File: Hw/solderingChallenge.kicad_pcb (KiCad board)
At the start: 2 copper layers, 13 parts, among them U1 ATtiny85-20SU

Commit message: Update connections
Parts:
- added J1: ISP, Connector_PinHeader_2.54mm:PinHeader_2x03_P2.54mm_Vertical, F.Cu at (139.9, 92.3)
- added TP1: PB0, TestPoint:TestPoint_Pad_1.0x1.0mm, F.Cu at (142.1, 81.2)
- added TP10: GND, Connectors_EC:TestPoint_Pad_1.0x1.0mm, F.Cu at (155.5, 73.5)
- added TP2: PB1, Connectors_EC:TestPoint_Pad_1.0x1.0mm, F.Cu at (142.1, 78.8)
- added TP3: PB2, Connectors_EC:TestPoint_Pad_1.0x1.0mm, F.Cu at (142.1, 75.7)
- added TP4: PB3, Connectors_EC:TestPoint_Pad_1.0x1.0mm, F.Cu at (142.1, 83.6)
- added TP5: PB4, Connectors_EC:TestPoint_Pad_1.0x1.0mm, F.Cu at (142.1, 86.2)
- added TP6: GND, Connectors_EC:TestPoint_Pad_1.0x1.0mm, F.Cu at (153.5, 83.5)
- added TP7: GND, Connectors_EC:TestPoint_Pad_1.0x1.0mm, F.Cu at (153.5, 77.1)
- added TP8: GND, Connectors_EC:TestPoint_Pad_1.0x1.0mm, F.Cu at (153.5, 80.6)
- added TP9: GND, Connectors_EC:TestPoint_Pad_1.0x1.0mm, F.Cu at (153.5, 86.1)
- moved D1 6.29 mm to (144.5, 73.6), turned to 180 degrees
- moved D2 6.29 mm to (144.5, 77.1), turned to 180 degrees
- moved D3 6.29 mm to (144.5, 80.6), turned to 180 degrees
- moved D4 6.29 mm to (144.5, 83.6), turned to 180 degrees
- moved D5 6.29 mm to (144.5, 86.1), turned to 180 degrees
- moved R1 6.29 mm to (150.5, 73.6), turned to 180 degrees
- moved R2 6.29 mm to (150.5, 77.1), turned to 180 degrees
- moved R3 6.29 mm to (150.5, 80.6), turned to 180 degrees
- moved R4 6.29 mm to (150.5, 83.6), turned to 180 degrees
- moved R5 6.29 mm to (150.5, 86.1), turned to 180 degrees
- moved C1 1.81 mm to (138.2, 73.7)
- moved BT1 1.41 mm to (142.4, 79.2)
- moved U1 1.27 mm to (135.9, 78.8)
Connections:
- net /PB1 renamed /MISO
- D1 pad 2: /PB0 -> /PB2
- D3 pad 2: /PB2 -> /MOSI
- U1 pad 5: /PB0 -> /MOSI
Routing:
- net VCC: track 0.00 -> 75.1 mm, vias 0 -> 2
- net /PB2: track 0.00 -> 34.5 mm, vias 0 -> 2
- net /RST: track 0.00 -> 32.3 mm, vias 0 -> 2
- net /MISO: track 0.00 -> 31.0 mm, vias 0 -> 2
- net GND: track 0.00 -> 20.7 mm, vias 0 -> 5
- net /PB3: track 0.00 -> 18.5 mm
- net /MOSI: track 0.00 -> 16.8 mm, vias 0 -> 2
- net /PB4: track 0.00 -> 16.2 mm
- net Net-(D5-Pad1): track 0.00 -> 5.36 mm
- net Net-(D4-Pad1): track 0.00 -> 5.03 mm
- net Net-(D3-Pad1): track 0.00 -> 4.25 mm
- net Net-(D2-Pad1): track 0.00 -> 3.97 mm
- net Net-(D1-Pad1): track 0.00 -> 3.05 mm
- added copper zone on B.Cu, net GND
- added copper zone on F.Cu, net GND
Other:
- board outline added: 33.5 x 33.5 mm
- net class Default: trace_width 0.25 -> 0.35; via_dia 0.8 -> 1; via_drill 0.4 -> 0.6
- net class vcc added: clearance 0.3, trace_width 0.5, via_dia 1, via_drill 0.6
- rule trace_min: 0.2 -> 0.3
- board text added: "0201"
- board text added: "0402"
- board text added: "0603"
- board text added: "0805"
- board text added: "1206"

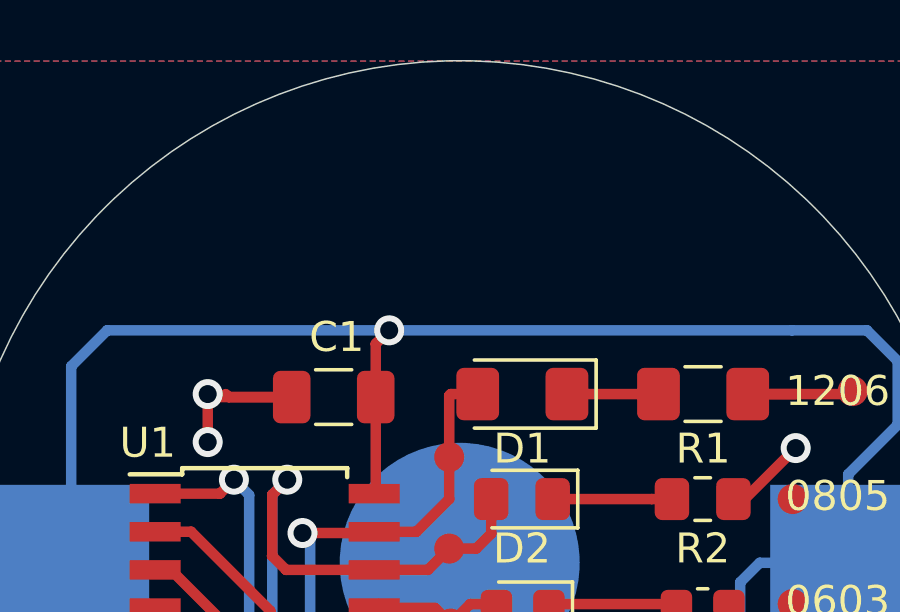
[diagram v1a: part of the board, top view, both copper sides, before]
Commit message: add logo wurth
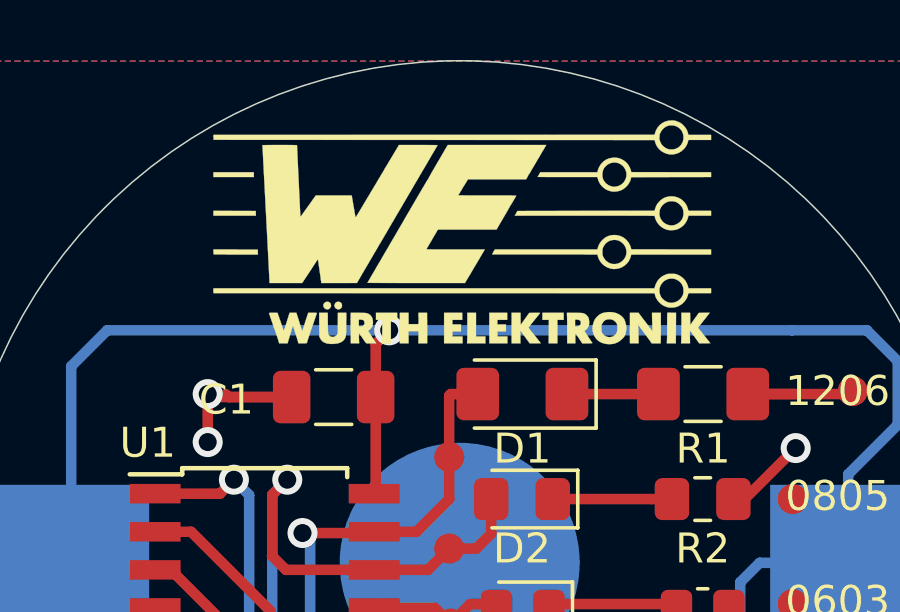
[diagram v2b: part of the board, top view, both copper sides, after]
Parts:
- added G***: LOGO, Aesthetics:wurth, F.Cu at (142.5, 68.2)

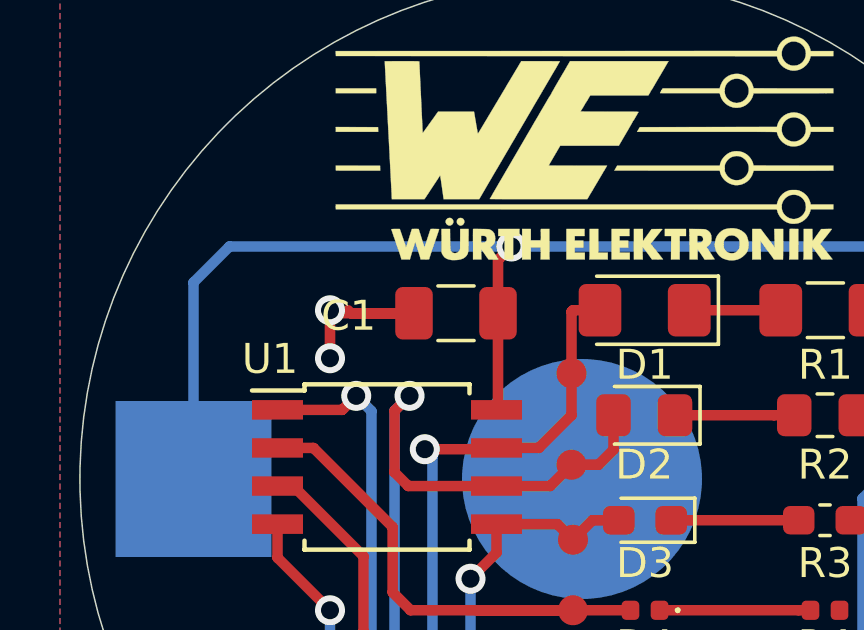
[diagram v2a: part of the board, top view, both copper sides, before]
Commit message: Change capacitor size
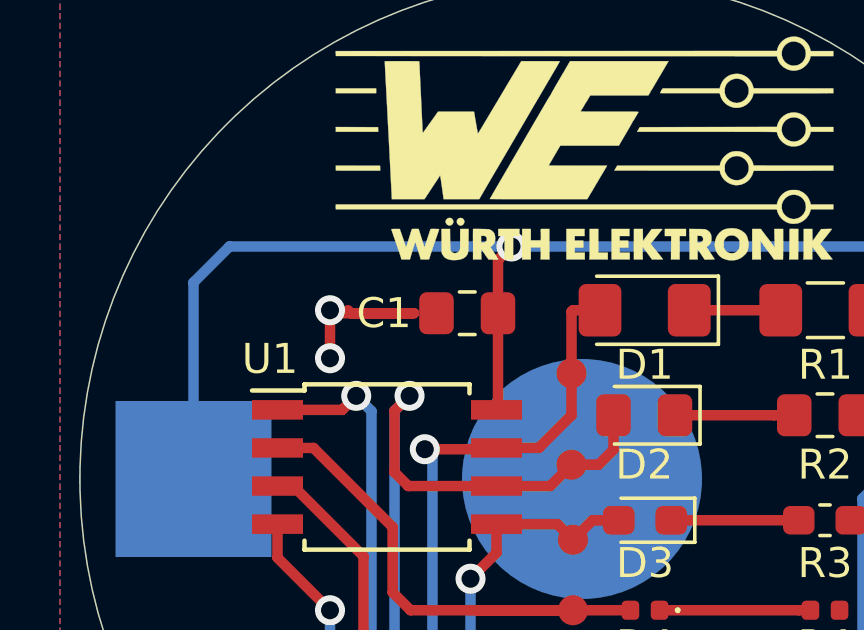
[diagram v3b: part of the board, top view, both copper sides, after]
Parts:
- C1: footprint Capacitor_SMD:C_1206_3216Metric -> Capacitor_SMD:C_0805_2012Metric_Pad1.15x1.40mm_HandSolder
- moved C1 0.38 mm to (138.6, 73.7)
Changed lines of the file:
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@@
-(kicad_pcb (version 20171130) (host pcbnew "(5.0.1-3-g963ef8bb5)")
+(kicad_pcb (version 20171130) (host pcbnew "(5.1.0-0)")
   (general
     (thickness 1.6)
@@
     (zone_45_only no)
     (trace_min 0.3)
-    (segment_width 0.2)
-    (edge_width 0.05)
     (via_size 1)
     (via_drill 0.6)
@@
     (uvia_min_size 0.2)
     (uvia_min_drill 0.1)
+    (edge_width 0.05)
+    (segment_width 0.2)
     (pcb_text_width 0.3)
     (pcb_text_size 1.5 1.5)
@@
     (uvia_dia 0.3)
     (uvia_drill 0.1)
+    (diff_pair_width 0.3)
     (diff_pair_gap 0.3)
-    (diff_pair_width 0.3)
     (add_net /MISO)
     (add_net /MOSI)
@@
     (uvia_dia 0.3)
     (uvia_drill 0.1)
+    (diff_pair_width 0.3)
     (diff_pair_gap 0.3)
-    (diff_pair_width 0.3)
+  )
+  (module Capacitor_SMD:C_0805_2012Metric_Pad1.15x1.40mm_HandSolder (layer F.Cu)
+    (at 138.575 73.7 180)
+    (descr "Capacitor SMD 0805 (2012 Metric), square (rectangular) end terminal, IPC_7351 nominal with elongated pad for handsoldering. (Body size source: https://docs.google.com/spreadsheets/d/1BsfQQcO9C6DZCsRaXUlFlo91Tg2WpOkGARC1WS5S8t0/edit?usp=sharing), generated with kicad-footprint-generator")
+    (tags "capacitor handsolder")
+    (attr smd)
+    (fp_text reference C1 (at 2.775 0 180) (layer F.SilkS)
+      (effects (font (size 1 1) (thickness 0.15)))
+    )
+    (fp_text value 0.1uF (at 0 1.65 180) (layer F.Fab)
+      (effects (font (size 1 1) (thickness 0.15)))
+    )
+    (fp_text user %R (at 0 0 180) (layer F.Fab)
+      (effects (font (size 0.5 0.5) (thickness 0.08)))
+    )
+    (fp_line (start 1.85 0.95) (end -1.85 0.95) (layer F.CrtYd) (width 0.05))
+    (fp_line (start 1.85 -0.95) (end 1.85 0.95) (layer F.CrtYd) (width 0.05))
+    (fp_line (start -1.85 -0.95) (end 1.85 -0.95) (layer F.CrtYd) (width 0.05))
+    (fp_line (start -1.85 0.95) (end -1.85 -0.95) (layer F.CrtYd) (width 0.05))
+    (fp_line (start -0.261252 0.71) (end 0.261252 0.71) (layer F.SilkS) (width 0.12))
+    (fp_line (start -0.261252 -0.71) (end 0.261252 -0.71) (layer F.SilkS) (width 0.12))
+    (fp_line (start 1 0.6) (end -1 0.6) (layer F.Fab) (width 0.1))
+    (fp_line (start 1 -0.6) (end 1 0.6) (layer F.Fab) (width 0.1))
+    (fp_line (start -1 -0.6) (end 1 -0.6) (layer F.Fab) (width 0.1))
+    (fp_line (start -1 0.6) (end -1 -0.6) (layer F.Fab) (width 0.1))
+    (pad 2 smd roundrect (at 1.025 0 180) (size 1.15 1.4) (layers F.Cu F.Paste F.Mask) (roundrect_rratio 0.217391)
+      (net 9 GND))
+    (pad 1 smd roundrect (at -1.025 0 180) (size 1.15 1.4) (layers F.Cu F.Paste F.Mask) (roundrect_rratio 0.217391)
+      (net 11 VCC))
+    (model ${KISYS3DMOD}/Capacitor_SMD.3dshapes/C_0805_2012Metric.wrl
+      (at (xyz 0 0 0))
+      (scale (xyz 1 1 1))
+      (rotate (xyz 0 0 0))
+    )
   )
   (module Connectors_EC:TestPoint_Pad_1.0x1.0mm (layer F.Cu)
@@
     )
   )
-  (module Capacitor_SMD:C_1206_3216Metric (layer F.Cu)
-    (at 138.2 73.7 180)
-    (descr "Capacitor SMD 1206 (3216 Metric), square (rectangular) end terminal, IPC_7351 nominal, (Body size source: http://www.tortai-tech.com/upload/download/2011102023233369053.pdf), generated with kicad-footprint-generator")
-    (tags capacitor)
-    (attr smd)
-    (fp_text reference C1 (at 3.58 -0.087 180) (layer F.SilkS)
-      (effects (font (size 1 1) (thickness 0.15)))
-    )
-    (fp_text value 0.1uF (at 0 1.82 180) (layer F.Fab)
-      (effects (font (size 1 1) (thickness 0.15)))
-    )
-    (fp_line (start -1.6 0.8) (end -1.6 -0.8) (layer F.Fab) (width 0.1))
-    (fp_line (start -1.6 -0.8) (end 1.6 -0.8) (layer F.Fab) (width 0.1))
-    (fp_line (start 1.6 -0.8) (end 1.6 0.8) (layer F.Fab) (width 0.1))
-    (fp_line (start 1.6 0.8) (end -1.6 0.8) (layer F.Fab) (width 0.1))
-    (fp_line (start -0.602064 -0.91) (end 0.602064 -0.91) (layer F.SilkS) (width 0.12))
-    (fp_line (start -0.602064 0.91) (end 0.602064 0.91) (layer F.SilkS) (width 0.12))
-    (fp_line (start -2.28 1.12) (end -2.28 -1.12) (layer F.CrtYd) (width 0.05))
-    (fp_line (start -2.28 -1.12) (end 2.28 -1.12) (layer F.CrtYd) (width 0.05))
-    (fp_line (start 2.28 -1.12) (end 2.28 1.12) (layer F.CrtYd) (width 0.05))
-    (fp_line (start 2.28 1.12) (end -2.28 1.12) (layer F.CrtYd) (width 0.05))
-    (fp_text user %R (at 0 0 180) (layer F.Fab)
-      (effects (font (size 0.8 0.8) (thickness 0.12)))
-    )
-    (pad 1 smd roundrect (at -1.4 0 180) (size 1.25 1.75) (layers F.Cu F.Paste F.Mask) (roundrect_rratio 0.2)
-      (net 11 VCC))
-    (pad 2 smd roundrect (at 1.4 0 180) (size 1.25 1.75) (layers F.Cu F.Paste F.Mask) (roundrect_rratio 0.2)
-      (net 9 GND))
-    (model ${KISYS3DMOD}/Capacitor_SMD.3dshapes/C_1206_3216Metric.wrl
-      (at (xyz 0 0 0))
-      (scale (xyz 1 1 1))
-      (rotate (xyz 0 0 0))
-    )
-  )

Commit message: Update version
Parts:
- removed D5: 0201, LED_SMD:LED_0201_0603Metric
- removed the G*** at (142.5, 68.2)
- removed R5: 0201, Resistor_SMD:R_0201_0603Metric
- removed TP5: PB4, Connectors_EC:TestPoint_Pad_1.0x1.0mm
- removed TP9: GND, Connectors_EC:TestPoint_Pad_1.0x1.0mm
- added G***: LOGO, Aesthetics:wurth, B.Cu at (133.6, 88.9)
- added G***: LOGO, Aesthetics:wurth, F.Cu at (133.3, 85.2)
- added G***: LOGO, Aesthetics:electronic_cats_logo_4x3, F.Cu at (150.4, 88.2)
- added G***: LOGO, Aesthetics:makersGDL, B.Cu at (142.0, 65.1)
- added G***: LOGO, Aesthetics:mouser, B.Cu at (151.4, 89.1)
- added G***: LOGO, Aesthetics:mouser, F.Cu at (137.8, 69.1)
- added G***: LOGO, Aesthetics:electronic_cats_logo_4x3, B.Cu at (142.6, 92.3)
- added G***: LOGO, Aesthetics:makersGDL, F.Cu at (150.2, 69.0)
- moved TP1 0.66 mm to (142.0, 80.6)
- moved TP2 0.35 mm to (142.0, 78.4)
- moved TP3 0.21 mm to (142.0, 75.5)
- moved TP4 0.10 mm to (142.0, 83.6)
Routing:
- net GND: track 20.7 -> 44.1 mm, vias 5 -> 6
- net /PB4: track 16.2 -> 0.00 mm
- net /MISO: track 31.0 -> 24.8 mm
- net Net-(D5-Pad1): track 5.36 -> 0.00 mm
- net /PB2: track 34.5 -> 38.4 mm
- net VCC: track 75.1 -> 74.0 mm
- net /MOSI: track 16.8 -> 17.7 mm
- net /PB3: track 18.5 -> 19.3 mm
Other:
- board text added: "Soldering Challenge"
- board text removed: "0201"

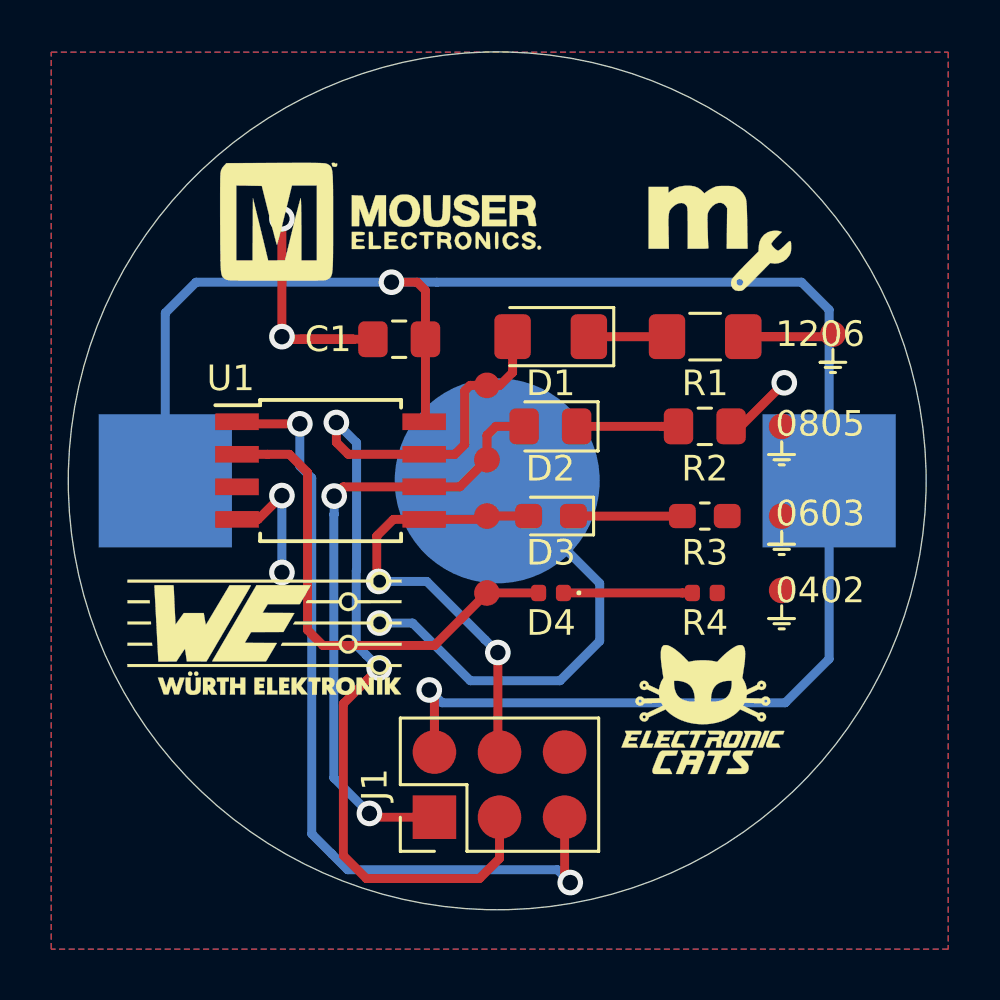
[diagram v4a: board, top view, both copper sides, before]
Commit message: Update logos and version
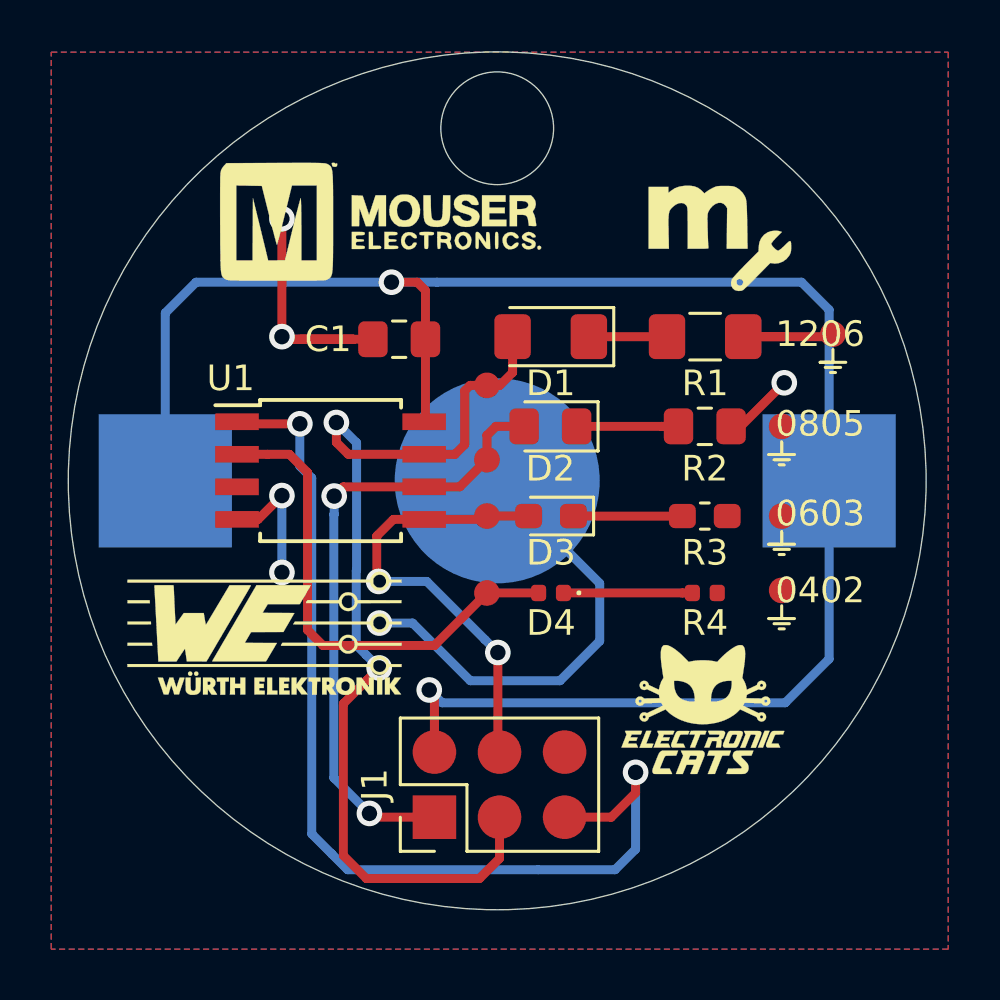
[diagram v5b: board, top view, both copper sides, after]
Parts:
- moved G*** 14.1 mm to (130.4, 73.0)
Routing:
- net /RST: track 32.2 -> 39.2 mm
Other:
- outline, holes or cut-outs redrawn
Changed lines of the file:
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@@
   (general
     (thickness 1.6)
-    (drawings 26)
-    (tracks 132)
+    (drawings 27)
+    (tracks 135)
     (zones 0)
     (modules 28)
@@
   (title_block
     (title "Soldering challenge")
-    (date 2019-04-09)
+    (date 2019-04-10)
     (rev v0.2)
     (company "Electronic Cats")
@@
   )
   (module Aesthetics:makersGDL (layer B.Cu)
-    (at 142.025 65.1 180)
+    (at 130.4 73 180)
     (fp_text reference G*** (at 0 0 180) (layer B.SilkS) hide
       (effects (font (size 1.524 1.524) (thickness 0.3)) (justify mirror))
@@
     )
   )
+  (gr_circle (center 142.4 65.468333) (end 144.6 65.468333) (layer Edge.Cuts) (width 0.05))
   (gr_line (start 155.4 75) (end 155.6 75) (layer F.SilkS) (width 0.12))
   (gr_line (start 155 74.6) (end 156 74.6) (layer F.SilkS) (width 0.12))
@@
   (segment (start 134.7 77) (end 134.7 78.65) (width 0.35) (layer B.Cu) (net 9))
   (segment (start 135.16399 92.99999) (end 135.16399 79.11399) (width 0.35) (layer B.Cu) (net 9))
-  (via (at 145.25 94.9) (size 1) (drill 0.6) (layers F.Cu B.Cu) (net 9))
-  (segment (start 145.03 94.68) (end 145.25 94.9) (width 0.35) (layer F.Cu) (net 9))
-  (segment (start 145.03 92.35) (end 145.03 94.68) (width 0.35) (layer F.Cu) (net 9))
   (segment (start 136.564001 94.400001) (end 135.9445 93.7805) (width 0.35) (layer B.Cu) (net 9))
-  (segment (start 144.750001 94.400001) (end 136.564001 94.400001) (width 0.35) (layer B.Cu) (net 9))
   (segment (start 135.9445 93.7805) (end 135.16399 92.99999) (width 0.35) (layer B.Cu) (net 9))
-  (segment (start 145.25 94.9) (end 144.750001 94.400001) (width 0.35) (layer B.Cu) (net 9))
+  (segment (start 145.03 92.35) (end 146.85 92.35) (width 0.35) (layer F.Cu) (net 9))
+  (via (at 147.8 90.6) (size 1) (drill 0.6) (layers F.Cu B.Cu) (net 9))
+  (segment (start 147.8 91.4) (end 147.8 90.6) (width 0.35) (layer F.Cu) (net 9))
+  (segment (start 146.85 92.35) (end 147.8 91.4) (width 0.35) (layer F.Cu) (net 9))
+  (segment (start 147.8 90.6) (end 147.8 93.6) (width 0.35) (layer B.Cu) (net 9))
+  (segment (start 146.999999 94.400001) (end 147.8 93.6) (width 0.35) (layer B.Cu) (net 9))
+  (segment (start 144.000001 94.400001) (end 146.999999 94.400001) (width 0.35) (layer B.Cu) (net 9))
+  (segment (start 144.000001 94.400001) (end 136.564001 94.400001) (width 0.35) (layer B.Cu) (net 9))
   (segment (start 129.45 72.675) (end 129.45 79.225) (width 0.35) (layer B.Cu) (net 10))
   (segment (start 130.65 71.475) (end 129.45 72.675) (width 0.35) (layer B.Cu) (net 10))

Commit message: V1.0
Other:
- board text added: "V1.0"
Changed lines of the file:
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@@
   (general
     (thickness 1.6)
-    (drawings 27)
+    (drawings 28)
     (tracks 135)
     (zones 0)
@@
     (title "Soldering challenge")
     (date 2019-04-10)
-    (rev v0.2)
+    (rev v1.0)
     (company "Electronic Cats")
     (comment 1 "Eduardo Contreras")
@@
     )
   )
+  (gr_text V1.0 (at 142.4 86.8) (layer B.SilkS)
+    (effects (font (size 1.5 1.5) (thickness 0.3)) (justify mirror))
+  )
   (gr_circle (center 142.4 65.468333) (end 144.6 65.468333) (layer Edge.Cuts) (width 0.05))
